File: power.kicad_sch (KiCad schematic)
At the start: 12 parts, among them Q1 Si2312BDS, U1 TLE2426xP, U2 TPS7250

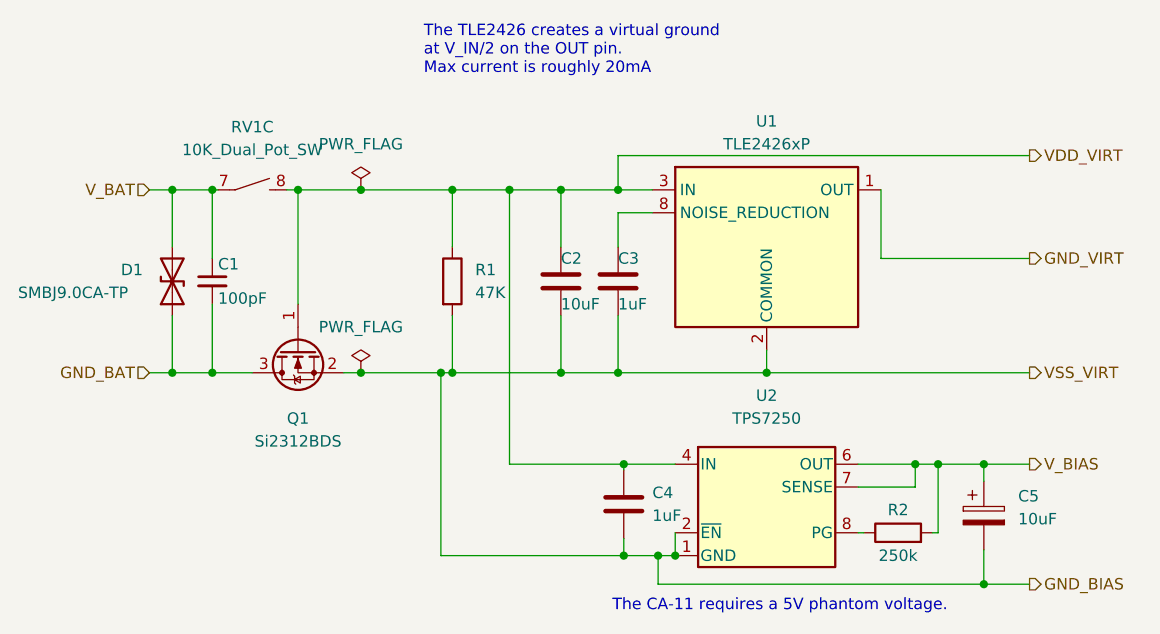
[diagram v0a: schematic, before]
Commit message: Finished placing refdes, fix DRC errors
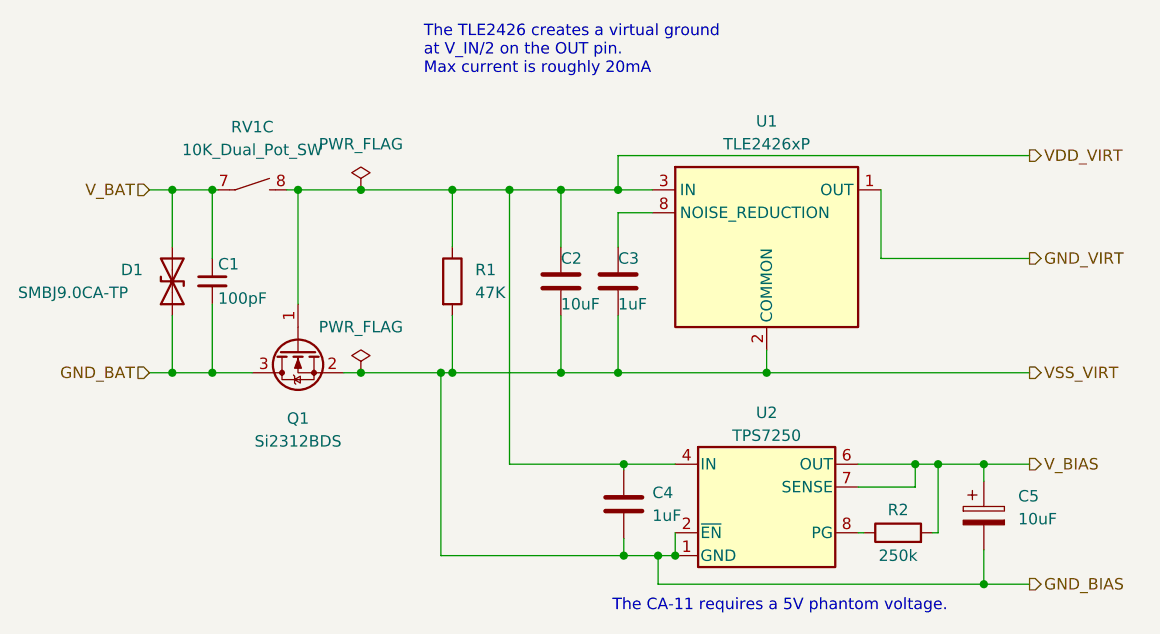
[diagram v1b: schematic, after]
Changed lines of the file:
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@@
   )
   (symbol (lib_id "preamp_lib:TPS7250") (at 129.54 106.68 0) (unit 1)
-    (in_bom yes) (on_board yes) (dnp no) (fields_autoplaced)
-    (property "Reference" "U2" (at 129.54 93.98 0)
+    (in_bom yes) (on_board yes) (dnp no)
+    (property "Reference" "U2" (at 129.54 95.885 0)
       (effects (font (size 1.27 1.27)))
     )
-    (property "Value" "TPS7250" (at 129.54 96.52 0)
+    (property "Value" "TPS7250" (at 129.54 98.425 0)
       (effects (font (size 1.27 1.27)))
     )
